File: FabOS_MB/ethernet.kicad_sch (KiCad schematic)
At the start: 4 parts, among them J3 RJ45, U7 CND-tek B1601S, U8 LAN8742A, U9 USBLC6-4SC6

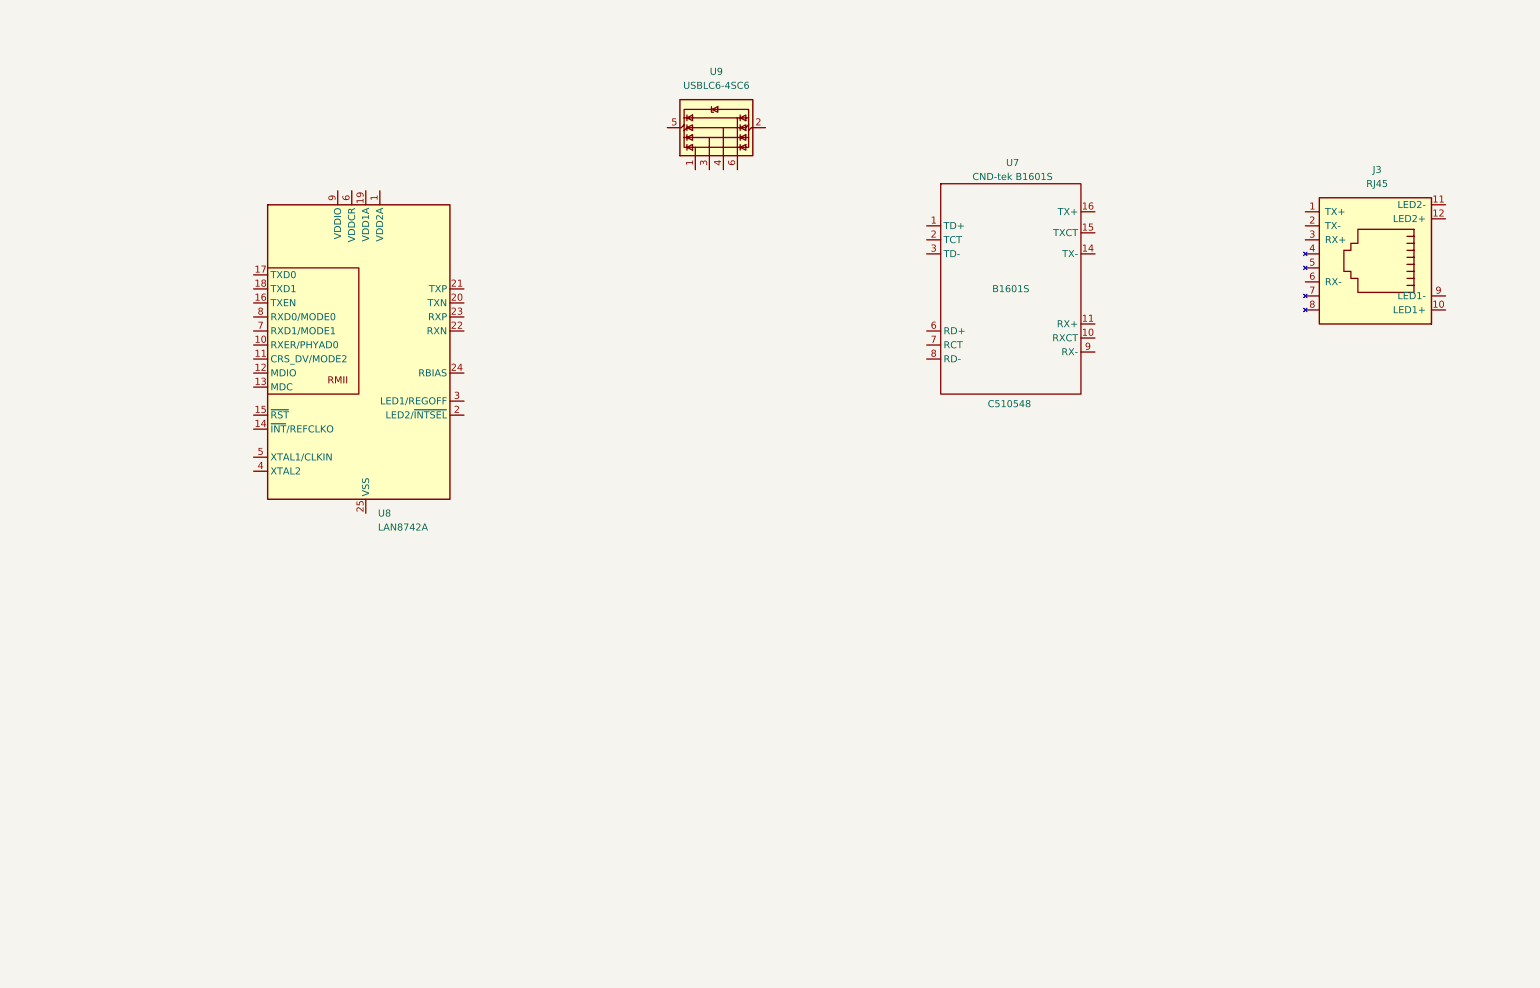
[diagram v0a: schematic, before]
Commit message: ethernet presque fini
resste pb avec certains composants : oscillateur et condensateur avec nom particuliers sur la doc difficilement trouvable
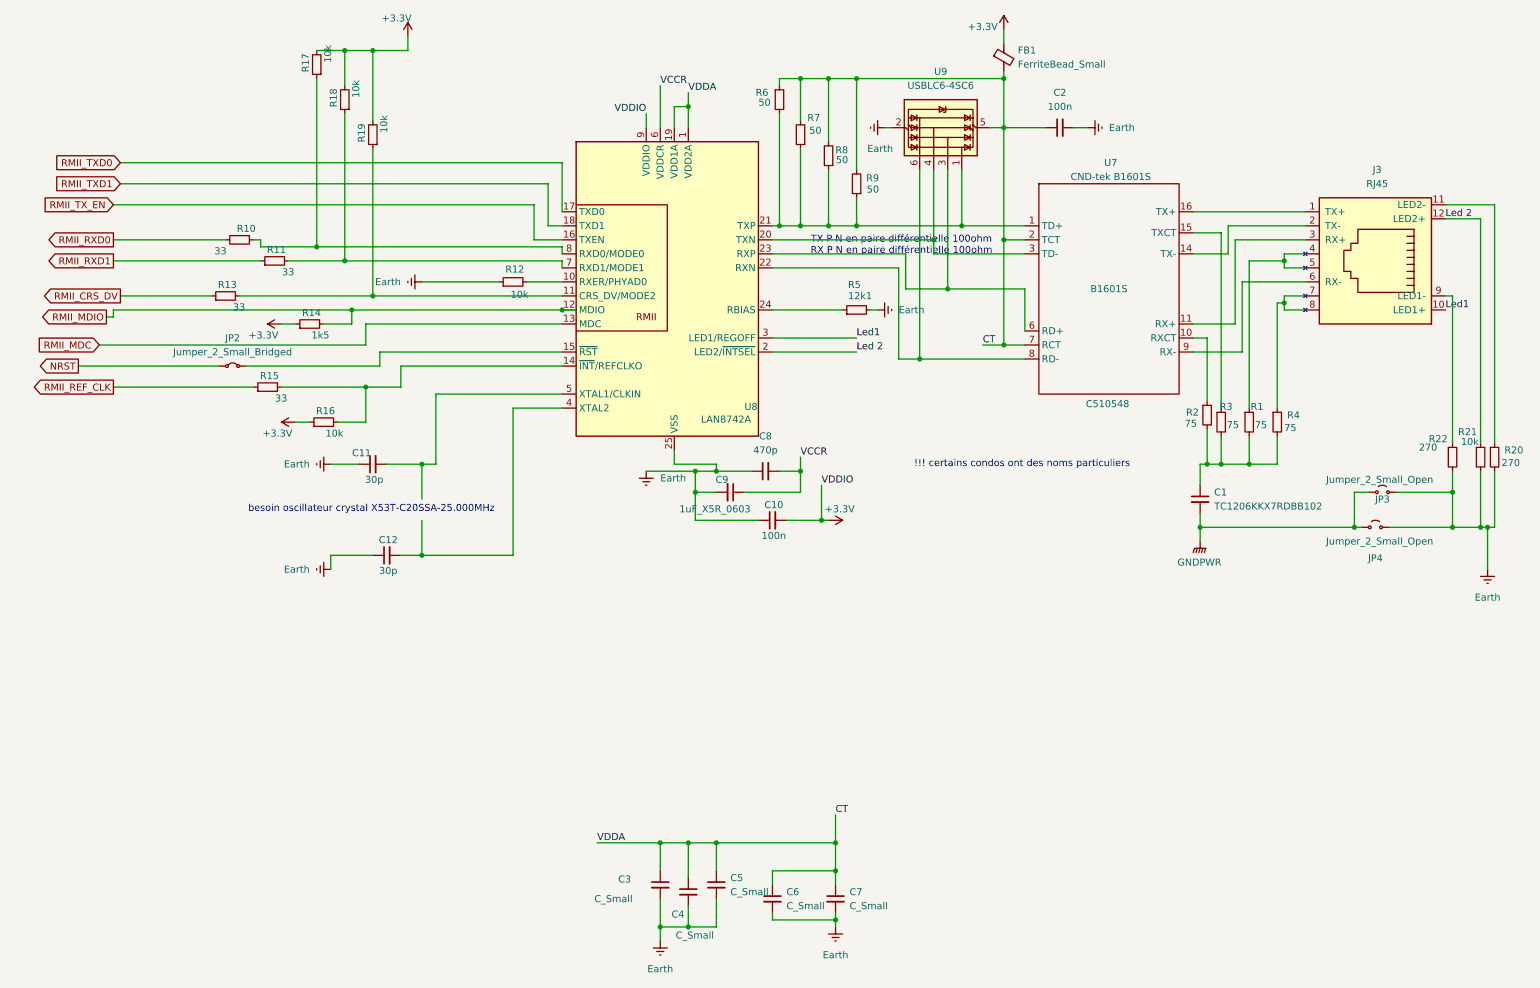
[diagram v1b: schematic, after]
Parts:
- added C1: TC1206KKX7RDBB102, symbol Device:C_Small
- added C10, C2: 100n, symbol Device:C_Small
- added C11, C12: 30p, symbol Device:C_Small
- added C3, C4, C5, C6, C7: C_Small, symbol Device:C_Small
- added C8: 470p, symbol Device:C_Small
- added C9: 1uF_X5R_0603, symbol Device:C_Small
- added FB1: FerriteBead_Small, symbol Device:FerriteBead_Small
- added JP2: Jumper_2_Small_Bridged, symbol Jumper:Jumper_2_Small_Bridged
- added JP3, JP4: Jumper_2_Small_Open, symbol Jumper:Jumper_2_Small_Open
- added R1, R2, R3, R4: 75, symbol Device:R_Small
- added R10, R11, R13, R15: 33, symbol Device:R_Small
- added R12, R16, R17, R18, R19, R21: 10k, symbol Device:R_Small
- added R14: 1k5, symbol Device:R_Small
- added R20, R22: 270, symbol Device:R_Small
- added R5: 12k1, symbol Device:R_Small
- added R6, R7, R8, R9: 50, symbol Device:R_Small
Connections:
- net at U9.1 (I/O1): now also U7.1 (TD+), U8.21 (TXP), R6.2, R7.1, R8.1, R9.1
- net Earth: now reaches U9.2 (GND)
- net Earth: now also U8.25 (VSS), C10.1, C11.1, C12.1, C2.2, C3.2, C4.2, C5.2, C6.2, C7.2, C8.1, C9.2, JP3.2 (B), JP4.2 (B), R12.1, R20.2, R21.2, R22.2, R5.2
- net at U9.3 (I/O2): now also U7.6 (RD+), U8.23 (RXP)
- net at U9.4 (I/O3): now also U7.3 (TD-), U8.20 (TXN)
- net CT: now reaches U9.5 (VBUS)
- net CT: now also U7.2 (TCT), U7.7 (RCT), U8.1 (VDD2A), U8.19 (VDD1A), C2.1, C3.1, C4.1, C5.1, C6.1, C7.1, FB1.2, R6.1, R7.2, R8.2, R9.2
- net at U9.6 (I/O4): now also U7.8 (RD-), U8.22 (RXN)
- net at U7.10 (RXCT): now also R2.1
- net at U7.11 (RX+): now also J3.3 (RX+)
- net at U7.14 (TX-): now also J3.2 (TX-)
- net at U7.15 (TXCT): now also R3.1
- net at U7.16 (TX+): now also J3.1 (TX+)
- net at U7.9 (RX-): now also J3.6 (RX-)
- net at U8.10 (RXER/PHYAD0): now also R12.2
- net at U8.11 (CRS_DV/MODE2): now also R13.2, R19.1
- net RMII_MDIO: now reaches U8.12 (MDIO)
- net RMII_MDIO: now also R14.2
- net RMII_MDC: now reaches U8.13 (MDC)
- net at U8.14 (~{INT}/REFCLKO): now also R15.2, R16.2
- net at U8.15 (~{RST}): now also JP2.2 (B)
- net RMII_TX_EN: now reaches U8.16 (TXEN)
- net RMII_TXD0: now reaches U8.17 (TXD0)
- net RMII_TXD1: now reaches U8.18 (TXD1)
- net Led 2: now reaches U8.2 (LED2/~{INTSEL})
- net Led 2: now also J3.12 (LED2+), R21.1
- net at U8.24 (RBIAS): now also R5.1
- net Led1: now reaches U8.3 (LED1/REGOFF)
- net Led1: now also J3.10 (LED1+)
- net at U8.4 (XTAL2): now also C12.2
- net at U8.5 (XTAL1/CLKIN): now also C11.2
- net VCCR: now reaches U8.6 (VDDCR)
- net VCCR: now also C8.2, C9.1
- net at U8.7 (RXD1/MODE1): now also R11.2, R18.1
- net at U8.8 (RXD0/MODE0): now also R10.1, R17.1
- net +3.3V: now reaches U8.9 (VDDIO)
- net +3.3V: now also C10.2, FB1.1, R14.1, R16.1, R17.2, R18.2, R19.2
- net at J3.11 (LED2-): now also R20.1
- net at J3.4: now also J3.5, R1.1
- net at J3.7: now also J3.8, R4.1
- net at J3.9 (LED1-): now also R22.1
- new net: C1.1, R1.2, R2.2, R3.2, R4.2
- new net GNDPWR: C1.2, JP3.1 (A), JP4.1 (A)
- new net NRST: JP2.1 (A)
- new net RMII_CRS_DV: R13.1
- new net RMII_REF_CLK: R15.1
- new net RMII_RXD0: R10.2
- new net RMII_RXD1: R11.1
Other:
- note added: "!!! certains condos ont des noms particuliers"
- note added: "TX P N en paire différentielle 100ohm RX P N en paire différentielle 100ohm"
- note added: "besoin oscillateur crystal X53T-C20SSA-25.000MHz"
- moved on the sheet: U7, U8, U9

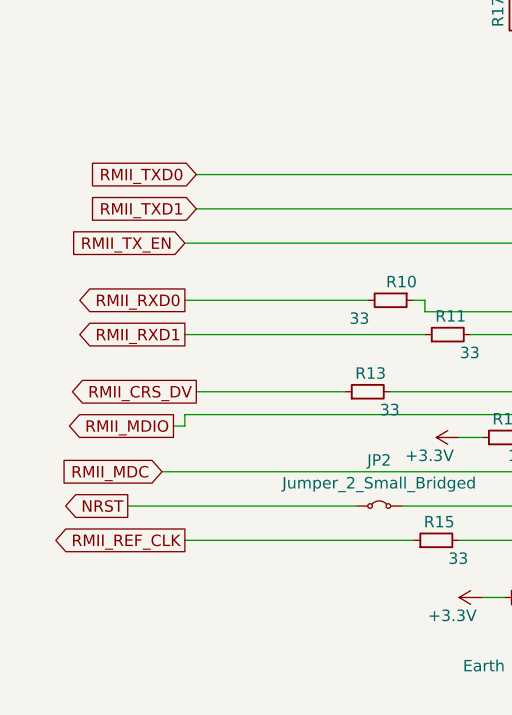
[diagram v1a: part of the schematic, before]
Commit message: ethernet pins hiérarchiques
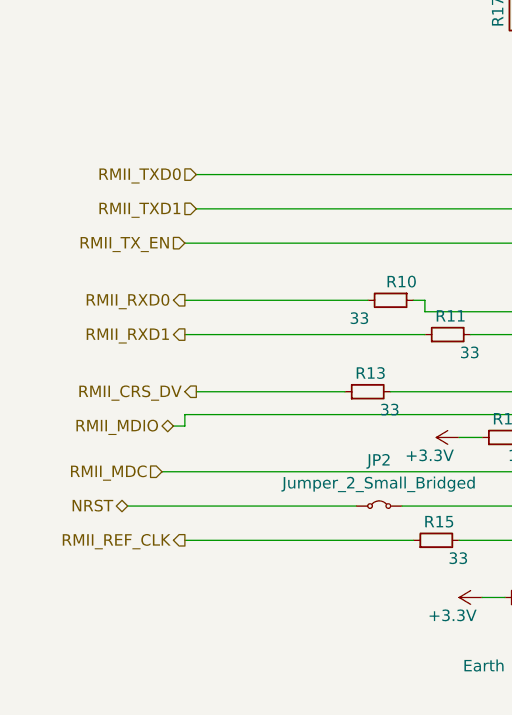
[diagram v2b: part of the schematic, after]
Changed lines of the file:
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@@
 		)
 	)
-	(global_label "NRST"
-		(shape output)
-		(at 21.59 77.47 180)
+	(hierarchical_label "RMII_MDIO"
+		(shape bidirectional)
+		(at 26.67 68.58 180)
 		(fields_autoplaced yes)
 		(effects
@@
 			(justify right)
 		)
-		(property "Intersheetrefs" "${INTERSHEET_REFS}"
-			(at 13.8272 77.47 0)
-			(effects
-				(font
-					(size 1.27 1.27)
-				)
-				(justify right)
-				(hide yes)
-			)
-		)
 	)
-	(global_label "RMII_TXD0"
+	(hierarchical_label "RMII_TXD0"
 		(shape input)
 		(at 29.21 40.64 180)
@@
 			(justify right)
 		)
-		(property "Intersheetrefs" "${INTERSHEET_REFS}"
-			(at 16.6696 40.64 0)
-			(effects
-				(font
-					(size 1.27 1.27)
-				)
-				(justify right)
-				(hide yes)
+	)
+	(hierarchical_label "RMII_TX_EN"
+		(shape input)
+		(at 27.94 48.26 180)
+		(fields_autoplaced yes)
+		(effects
+			(font
+				(size 1.27 1.27)
 			)
+			(justify right)
 		)
 	)
-	(global_label "RMII_REF_CLK"
+	(hierarchical_label "RMII_MDC"
+		(shape input)
+		(at 25.4 73.66 180)
+		(fields_autoplaced yes)
+		(effects
+			(font
+				(size 1.27 1.27)
+			)
+			(justify right)
+		)
+	)
+	(hierarchical_label "NRST"
+		(shape bidirectional)
+		(at 21.59 77.47 180)
+		(fields_autoplaced yes)
+		(effects
+			(font
+				(size 1.27 1.27)
+			)
+			(justify right)
+		)
+	)
+	(hierarchical_label "RMII_RXD0"
+		(shape output)
+		(at 27.94 54.61 180)
+		(fields_autoplaced yes)
+		(effects
+			(font
+				(size 1.27 1.27)
+			)
+			(justify right)
+		)
+	)
+	(hierarchical_label "RMII_TXD1"
+		(shape input)
+		(at 29.21 44.45 180)
+		(fields_autoplaced yes)
+		(effects
+			(font
+				(size 1.27 1.27)
+			)
+			(justify right)
+		)
+	)
+	(hierarchical_label "RMII_REF_CLK"
 		(shape output)
 		(at 27.94 81.28 180)
@@
 			(justify right)
 		)
-		(property "Intersheetrefs" "${INTERSHEET_REFS}"
-			(at 12.0129 81.28 0)
-			(effects
-				(font
-					(size 1.27 1.27)
-				)
-				(justify right)
-				(hide yes)
-			)
-		)
 	)
-	(global_label "RMII_RXD1"
+	(hierarchical_label "RMII_RXD1"
 		(shape output)
 		(at 27.94 58.42 180)
@@
 			(justify right)
 		)
-		(property "Intersheetrefs" "${INTERSHEET_REFS}"
-			(at 15.0972 58.42 0)
-			(effects
-				(font
-					(size 1.27 1.27)
-				)
-				(justify right)
-				(hide yes)
-			)
-		)
 	)
-	(global_label "RMII_CRS_DV"
+	(hierarchical_label "RMII_CRS_DV"
 		(shape output)
 		(at 29.21 64.77 180)
@@
 			(justify right)
 		)
-		(property "Intersheetrefs" "${INTERSHEET_REFS}"
-			(at 14.2505 64.77 0)
-			(effects
-				(font
-					(size 1.27 1.27)
-				)
-				(justify right)
-				(hide yes)
-			)
-		)
 	)
-	(global_label "RMII_MDC"
-		(shape input)
-		(at 25.4 73.66 180)
-		(fields_autoplaced yes)
-		(effects
-			(font
-				(size 1.27 1.27)
-			)
-			(justify right)
-		)
-		(property "Intersheetrefs" "${INTERSHEET_REFS}"
-			(at 13.5248 73.66 0)
-			(effects
-				(font
-					(size 1.27 1.27)
-				)
-				(justify right)
-				(hide yes)
-			)
-		)
-	)
-	(global_label "RMII_MDIO"
-		(shape output)
-		(at 26.67 68.58 180)
-		(fields_autoplaced yes)
-		(effects
-			(font
-				(size 1.27 1.27)
-			)
-			(justify right)
-		)
-		(property "Intersheetrefs" "${INTERSHEET_REFS}"
-			(at 14.1295 68.58 0)
-			(effects
-				(font
-					(size 1.27 1.27)
-				)
-				(justify right)
-				(hide yes)
-			)
-		)
-	)
-	(global_label "RMII_TXD1"
-		(shape input)
-		(at 29.21 44.45 180)
-		(fields_autoplaced yes)
-		(effects
-			(font
-				(size 1.27 1.27)
-			)
-			(justify right)
-		)
-		(property "Intersheetrefs" "${INTERSHEET_REFS}"
-			(at 16.6696 44.45 0)
-			(effects
-				(font
-					(size 1.27 1.27)
-				)
-				(justify right)
-				(hide yes)
-			)
-		)
-	)
-	(global_label "RMII_TX_EN"
-		(shape input)
-		(at 27.94 48.26 180)
-		(fields_autoplaced yes)
-		(effects
-			(font
-				(size 1.27 1.27)
-			)
-			(justify right)
-		)
-		(property "Intersheetrefs" "${INTERSHEET_REFS}"
-			(at 14.432 48.26 0)
-			(effects
-				(font
-					(size 1.27 1.27)
-				)
-				(justify right)
-				(hide yes)
-			)
-		)
-	)
-	(global_label "RMII_RXD0"
-		(shape output)
-		(at 27.94 54.61 180)
-		(fields_autoplaced yes)
-		(effects
-			(font
-				(size 1.27 1.27)
-			)
-			(justify right)
-		)
-		(property "Intersheetrefs" "${INTERSHEET_REFS}"
-			(at 15.0972 54.61 0)
-			(effects
-				(font
-					(size 1.27 1.27)
-				)
-				(justify right)
-				(hide yes)
-			)
-		)
-	)

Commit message: verif
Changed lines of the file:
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@@
 		)
 		(property "Value" "1uF_X5R_0603"
-			(at 136.906 103.378 90)
+			(at 138.684 103.886 90)
 			(effects
 				(font

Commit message: Maj schéma
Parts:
- renumbered C3 to C10, C4 to C11, C5 to C12, C9 to C13, C8 to C14, C10 to C15, C6 to C16, C7 to C17, C2 to C18, C1 to C19, C11 to C8, C12 to C9, J3 to J1, JP2 to JP1, JP4 to JP2, R16 to R10, R18 to R11, R19 to R12, R12 to R13, R6 to R14, R7 to R15, R8 to R16, R9 to R17, R5 to R18, R2 to R19, R3 to R20, R1 to R21, R4 to R22, R22 to R23, R21 to R24, R20 to R25, R13 to R4, R10 to R5, R15 to R6, R11 to R7, R14 to R8, R17 to R9, U8 to U4, U9 to U5, U7 to U6
